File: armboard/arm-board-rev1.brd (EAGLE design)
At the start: 124.5 x 56.5 mm, 37 parts, among them J2_12V ANDERSON_POWERPOLEPP45_PCB_HO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, J2_GND ANDERSON_POWERPOLEPP45_PCB_HO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, X1 53261-06

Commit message: finished routing, FINAL REV1 PENDING PEER REVIEW
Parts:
- removed H1: MOUNT-HOLE3.2, holes:3,2
- DECAP: value (none) -> 1uF
- moved H2 57.7 mm to (82.5, 52.1)
- moved ENC_WI 11.1 mm to (118.7, 2.67)
- moved ENC_WO 11.1 mm to (108.6, 2.67)
- moved ENC_EI 11.1 mm to (98.4, 2.67)
- moved ENC_EO 11.1 mm to (88.3, 2.67)
- moved LED_XB_RX 6.35 mm to (93.3, 41.3)
- moved LED_XB_TX 6.35 mm to (95.9, 41.3)
- moved RES_LEDXBRX 6.35 mm to (93.3, 38.1)
- moved RES_LEDXBTX 6.35 mm to (95.9, 38.1)
- moved XB 6.35 mm to (78.7, 56.5)
- moved RES_LEDDYNASWD 5.43 mm to (111.1, 44.8), turned to 90 degrees
- moved MAX232_C2_1 5.08 mm to (18.7, 47.8)
- moved DECAP 5.08 mm to (29.2, 24.6)
- moved EE-12V 5.08 mm to (131.4, 28.8)
- moved EE-GND 5.08 mm to (131.4, 28.8)
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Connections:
- removed net N$5: MAX232_1.16, MAX232_DECAP_1.2
- net +3V3: now also MAX232_1.16, MAX232_DECAP_1.2
- net ENC_EI: now also U$1.PD1
- net ENC_EO: now also U$1.PD0
- net ENC_J1: now also U$1.PM2
- net ENC_J2: now also U$1.PM1
- net ENC_WI: now also U$1.PM3
- net ENC_WO: now also U$1.PL4
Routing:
- net DYNA_TX: track 36.9 -> 192.5 mm, vias 1 -> 3
- net J2_TTLRX: track 0.00 -> 80.4 mm
- net J2_TTLTX: track 0.00 -> 78.4 mm
- net +5V: track 0.00 -> 53.2 mm, vias 0 -> 14
- net +3V3: track 69.6 -> 117.2 mm, vias 1 -> 3
- net J2_RC1: track 0.00 -> 44.5 mm, vias 0 -> 1
- net ENC_EO: track 0.00 -> 23.2 mm
- net ENC_J1: track 0.00 -> 16.9 mm
- net ENC_EI: track 0.00 -> 14.5 mm
- net GND: track 18.6 -> 28.7 mm
- net ENC_J2: track 0.00 -> 9.56 mm
- net ENC_WO: track 0.00 -> 9.15 mm
- net ENC_WI: track 0.00 -> 4.51 mm
- net XB_RX: track 41.1 -> 37.3 mm
- net XB_TX: track 31.1 -> 27.3 mm
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- added copper zone on layer 16, net +5V
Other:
- board size 124.5 x 56.5 mm -> 124.5 x 55.9 mm
- board text added: "CUT ALONG DOTTED LINE"
- board text added: "READ & WRITE WRITE"
- board text removed: "IDLE DYNA_RX DYNA_TX"

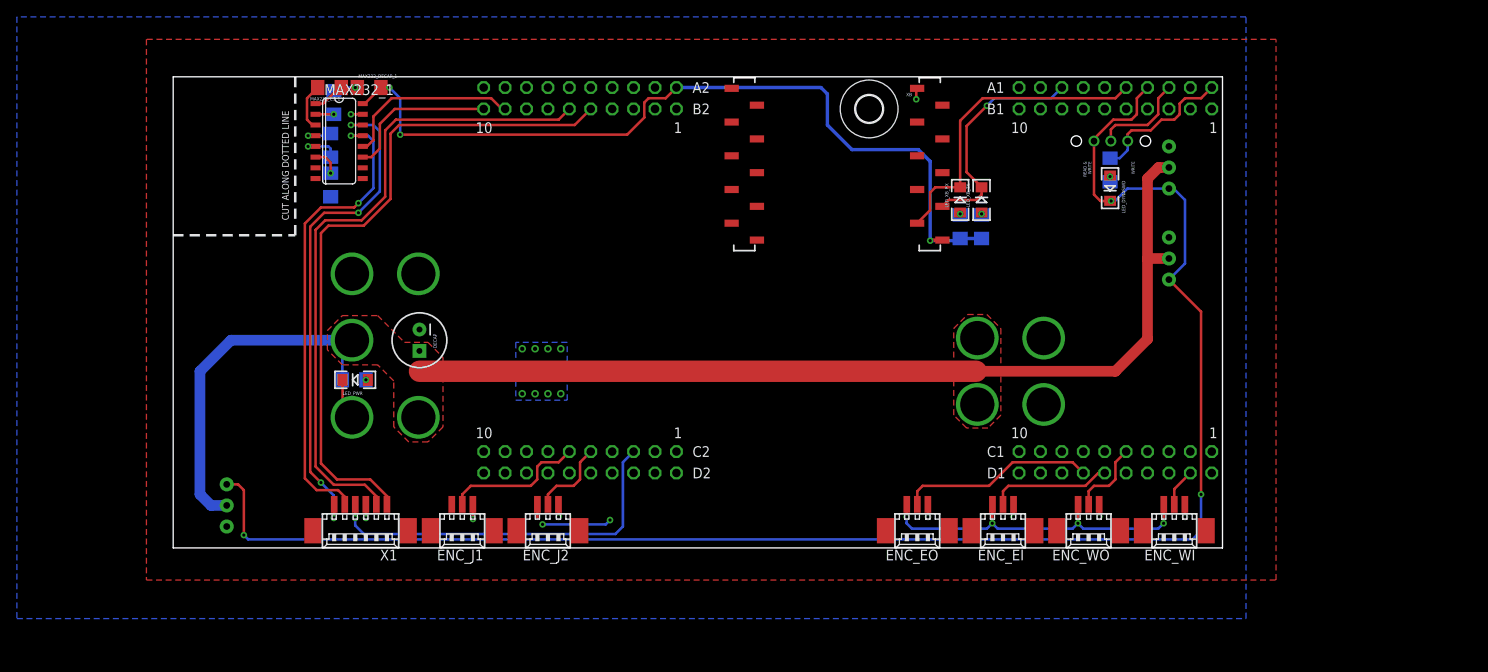
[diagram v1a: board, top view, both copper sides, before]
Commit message: added label/logo and 2 dio's to xbee
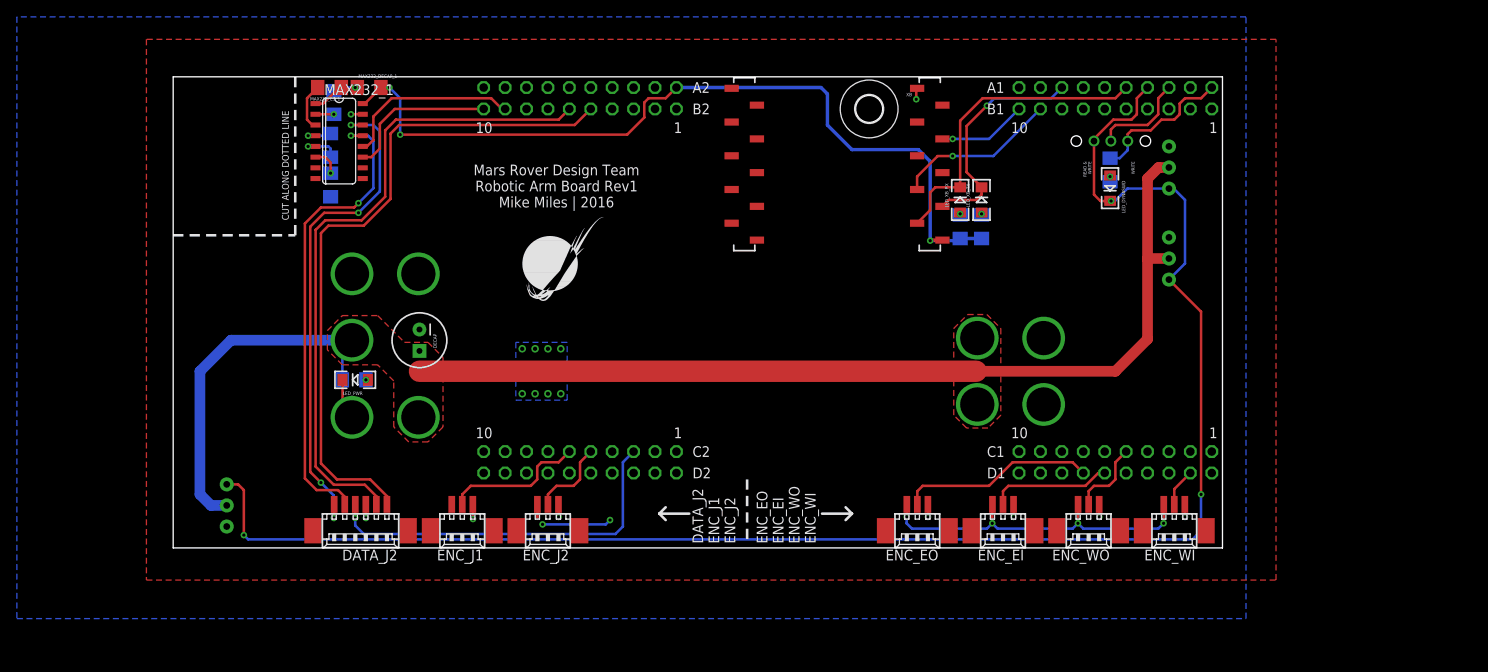
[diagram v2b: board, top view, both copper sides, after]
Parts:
- added U$3: (no value), MRDT-2015-General:MRDT_LOGO
- renumbered X1 to DATA_J2
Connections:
- net XB_DIO11: now also U$1.PM5
- net XB_DIO12: now also U$1.PM4
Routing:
- net XB_DIO12: track 0.00 -> 19.5 mm, vias 0 -> 1
- net XB_DIO11: track 0.00 -> 11.7 mm, vias 0 -> 1
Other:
- board text added: "DATA_J2 ENC_J1 ENC_J2 ENC_EO ENC_EI ENC_WO ENC_WI"
- board text added: "Mars Rover Design Team Robotic Arm Board Rev1 Mike Miles | 2016"
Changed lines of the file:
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@@
 <layer number="17" name="Pads" color="2" fill="1" visible="yes" active="yes"/>
 <layer number="18" name="Vias" color="2" fill="1" visible="yes" active="yes"/>
-<layer number="19" name="Unrouted" color="6" fill="1" visible="no" active="yes"/>
-<layer number="20" name="Dimension" color="5" fill="1" visible="no" active="yes"/>
-<layer number="21" name="tPlace" color="7" fill="1" visible="no" active="yes"/>
-<layer number="22" name="bPlace" color="7" fill="1" visible="no" active="yes"/>
-<layer number="23" name="tOrigins" color="15" fill="1" visible="no" active="yes"/>
-<layer number="24" name="bOrigins" color="15" fill="1" visible="no" active="yes"/>
-<layer number="25" name="tNames" color="7" fill="1" visible="no" active="yes"/>
-<layer number="26" name="bNames" color="7" fill="1" visible="no" active="yes"/>
+<layer number="19" name="Unrouted" color="6" fill="1" visible="yes" active="yes"/>
+<layer number="20" name="Dimension" color="5" fill="1" visible="yes" active="yes"/>
+<layer number="21" name="tPlace" color="7" fill="1" visible="yes" active="yes"/>
+<layer number="22" name="bPlace" color="7" fill="1" visible="yes" active="yes"/>
+<layer number="23" name="tOrigins" color="15" fill="1" visible="yes" active="yes"/>
+<layer number="24" name="bOrigins" color="15" fill="1" visible="yes" active="yes"/>
+<layer number="25" name="tNames" color="7" fill="1" visible="yes" active="yes"/>
+<layer number="26" name="bNames" color="7" fill="1" visible="yes" active="yes"/>
 <layer number="27" name="tValues" color="7" fill="1" visible="no" active="yes"/>
 <layer number="28" name="bValues" color="7" fill="1" visible="no" active="yes"/>
@@
 <layer number="49" name="Reference" color="7" fill="1" visible="no" active="yes"/>
 <layer number="50" name="dxf" color="7" fill="1" visible="no" active="yes"/>
-<layer number="51" name="tDocu" color="7" fill="1" visible="no" active="yes"/>
-<layer number="52" name="bDocu" color="7" fill="1" visible="no" active="yes"/>
+<layer number="51" name="tDocu" color="7" fill="1" visible="yes" active="yes"/>
+<layer number="52" name="bDocu" color="7" fill="1" visible="yes" active="yes"/>
 <layer number="91" name="Nets" color="2" fill="1" visible="no" active="no"/>
 <layer number="92" name="Busses" color="1" fill="1" visible="no" active="no"/>
@@
 <wire x1="14.478" y1="37.084" x2="14.478" y2="55.88" width="0.3048" layer="21" style="shortdash"/>
 <text x="13.716" y="38.862" size="0.8128" layer="21" rot="R90">CUT ALONG DOTTED LINE</text>
+<text x="76.2" y="0.508" size="1.27" layer="21" rot="R90">DATA_J2
+ENC_J1
+ENC_J2
+ENC_EO
+ENC_EI
+ENC_WO
+ENC_WI</text>
+<wire x1="68.072" y1="8.128" x2="68.072" y2="0.762" width="0.3048" layer="21" style="shortdash"/>
+<wire x1="61.214" y1="4.064" x2="57.658" y2="4.064" width="0.3048" layer="21"/>
+<wire x1="58.42" y1="3.302" x2="57.658" y2="4.064" width="0.3048" layer="21"/>
+<wire x1="57.658" y1="4.064" x2="58.42" y2="4.826" width="0.3048" layer="21"/>
+<wire x1="76.962" y1="4.064" x2="80.518" y2="4.064" width="0.3048" layer="21"/>
+<wire x1="79.756" y1="4.826" x2="80.518" y2="4.064" width="0.3048" layer="21"/>
+<wire x1="80.518" y1="4.064" x2="79.756" y2="3.302" width="0.3048" layer="21"/>
+<text x="45.466" y="42.926" size="1.27" layer="21" align="center">Mars Rover Design Team
+Robotic Arm Board Rev1
+Mike Miles | 2016</text>
 </plain>
 <attributes>
@@
 </element>
 <element name="H2" library="holes" package="3,2" value="MOUNT-HOLE3.2" x="82.55" y="52.07"/>
-<element name="X1" library="con-molex" package="53261-06" value="53261-06" x="22.225" y="2.667" rot="R180">
+<element name="DATA_J2" library="con-molex" package="53261-06" value="53261-06" x="22.225" y="2.667" rot="R180">
 <attribute name="OC_NEWARK" value="unknown" x="22.225" y="2.667" size="1.778" layer="27" rot="R180" display="off"/>
 <attribute name="MPN" value="" x="22.225" y="2.667" size="1.778" layer="27" rot="R180" display="off"/>
@@
 </element>
 <element name="U$2" library="MRDT-Electromechanical" package="C&amp;K-SS12D07VG4NSGAPA" value="SWITCH_SPDT_VERTSS12D07VG4NSGAPA" x="109.22" y="48.26"/>
+<element name="U$3" library="MRDT-2015-General" package="MRDT_LOGO" value="" x="41.402" y="28.448"/>
 </elements>
 <signals>
@@
 <contactref element="ENC_WO" pad="3"/>
 <contactref element="DECAP" pad="2"/>
-<contactref element="X1" pad="4"/>
+<contactref element="DATA_J2" pad="4"/>
 <contactref element="MAX232_VNCAP_1" pad="2"/>
 <contactref element="MAX232_VPCAP_1" pad="2"/>
@@
 <signal name="XB_DIO11">
 <contactref element="XB" pad="7"/>
+<contactref element="U$1" pad="PM5"/>
+<wire x1="91.24" y1="48.515" x2="90.679" y2="48.515" width="0.3048" layer="1"/>
+<wire x1="90.679" y1="48.515" x2="92.456" y2="48.514" width="0.3048" layer="1"/>
+<via x="92.456" y="48.514" extent="1-16" drill="0.381"/>
+<wire x1="92.456" y1="48.514" x2="96.774" y2="48.514" width="0.3048" layer="16"/>
+<wire x1="96.774" y1="48.514" x2="100.33" y2="52.07" width="0.3048" layer="16"/>
 </signal>
 <signal name="XB_RSSI">
@@
 <signal name="XB_DIO12">
 <contactref element="XB" pad="4"/>
+<contactref element="U$1" pad="PM4"/>
+<wire x1="88.24" y1="42.515" x2="88.24" y2="44.044" width="0.3048" layer="1"/>
+<wire x1="88.24" y1="44.044" x2="90.678" y2="46.482" width="0.3048" layer="1"/>
+<wire x1="90.678" y1="46.482" x2="92.456" y2="46.482" width="0.3048" layer="1"/>
+<via x="92.456" y="46.482" extent="1-16" drill="0.381"/>
+<wire x1="92.456" y1="46.482" x2="97.282" y2="46.482" width="0.3048" layer="16"/>
+<wire x1="97.282" y1="46.482" x2="102.87" y2="52.07" width="0.3048" layer="16"/>
 </signal>
 <signal name="+3V3">
@@
 <signal name="J2_RC1">
 <contactref element="U$1" pad="PK5"/>
-<contactref element="X1" pad="3"/>
+<contactref element="DATA_J2" pad="3"/>
 <wire x1="21.6" y1="5.167" x2="21.6" y2="3.566" width="0.3048" layer="1"/>
 <wire x1="21.6" y1="3.566" x2="21.59" y2="3.556" width="0.3048" layer="1"/>
@@
 </signal>
 <signal name="J2_TTLTX">
-<contactref element="X1" pad="5"/>
+<contactref element="DATA_J2" pad="5"/>
 <contactref element="U$1" pad="PK1"/>
 <wire x1="46.99" y1="52.07" x2="45.72" y2="50.8" width="0.3048" layer="1"/>
@@
 </signal>
 <signal name="J2_TTLRX">
-<contactref element="X1" pad="6"/>
+<contactref element="DATA_J2" pad="6"/>
 <contactref element="U$1" pad="PK0"/>
 <wire x1="49.53" y1="52.07" x2="47.625" y2="50.165" width="0.3048" layer="1"/>
@@
 </signal>
 <signal name="T1OUT">
-<contactref element="X1" pad="1"/>
+<contactref element="DATA_J2" pad="1"/>
 <contactref element="MAX232_1" pad="14"/>
 <wire x1="22.485" y1="50.165" x2="21.082" y2="50.165" width="0.3048" layer="1"/>
@@
 <signal name="R1IN">
 <contactref element="MAX232_1" pad="13"/>
-<contactref element="X1" pad="2"/>
+<contactref element="DATA_J2" pad="2"/>
 <wire x1="22.485" y1="48.895" x2="21.082" y2="48.895" width="0.3048" layer="1"/>
 <via x="21.082" y="48.895" extent="1-16" drill="0.381"/>

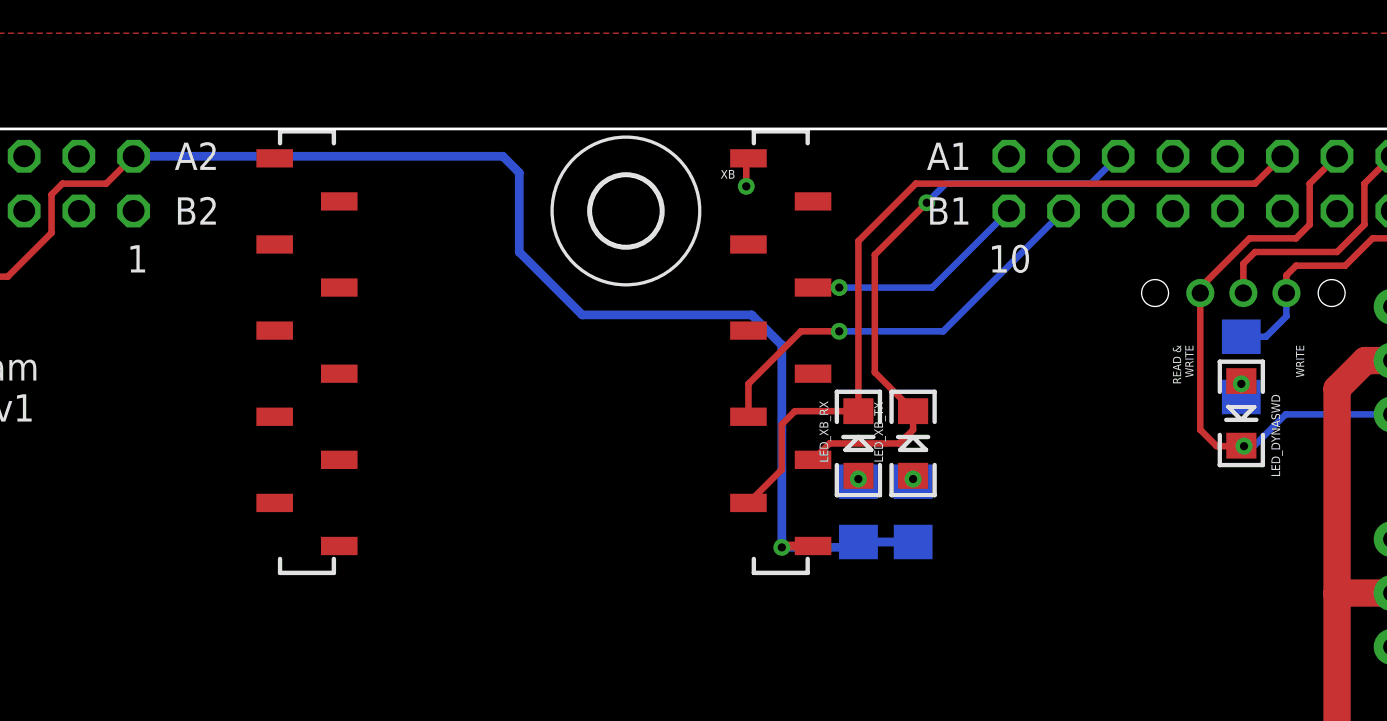
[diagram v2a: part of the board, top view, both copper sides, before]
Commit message: moved xbee in a little, reviewed by Drue on arm ; REV 1 FINAL of Gripper Board
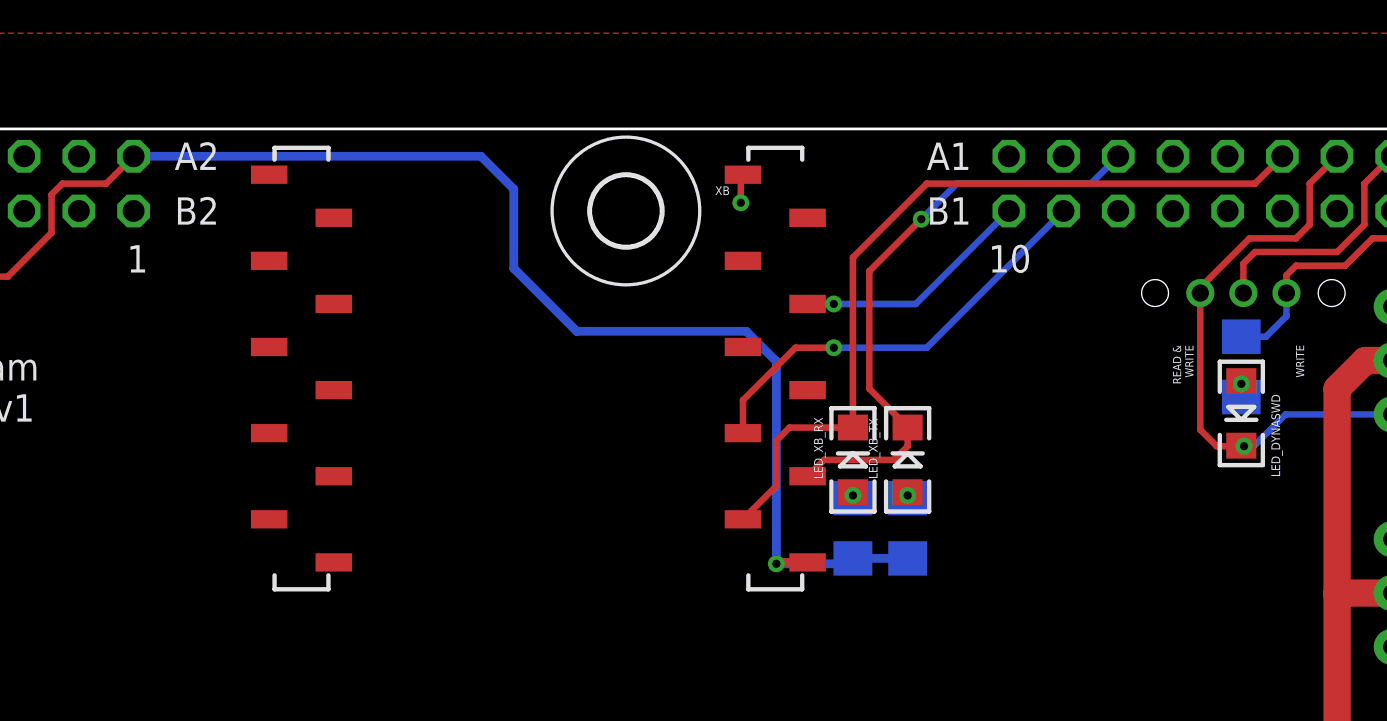
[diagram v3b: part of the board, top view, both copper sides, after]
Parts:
- moved LED_XB_RX 0.80 mm to (93.1, 40.5)
- moved LED_XB_TX 0.80 mm to (95.6, 40.5)
- moved RES_LEDXBRX 0.80 mm to (93.1, 37.3)
- moved RES_LEDXBTX 0.80 mm to (95.6, 37.3)
- moved XB 0.80 mm to (78.5, 55.8)
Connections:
- removed net TRI_EN: U$1.PB2
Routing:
- net XB_DIO11: track 11.7 -> 12.3 mm
- net XB_RX: track 37.3 -> 37.9 mm
- net XB_TX: track 27.3 -> 27.9 mm
- net XB_DIO12: track 19.5 -> 20.1 mm
